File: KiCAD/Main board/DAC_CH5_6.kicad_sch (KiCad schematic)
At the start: 51 parts, among them U1 PCM1789-Q1, U3 OPA1632DR, U4 OPA1632DR

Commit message: Worked a bit on the main board
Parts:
- removed R1 (x4): 22R, Resistor_SMD:R_0805_2012Metric, symbol Device:R
- removed unit 1 of U1
- added R100: 22R, Resistor_SMD:R_Array_Convex_4x0402, symbol Device:R_Pack04
- added unit 1 of U1
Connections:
- net +3.3V: now also U1.6 (VDD)
- net AMUTEI: now also U1.17 (AMUTEI)
- net BCK: now also R100.6 (R3.2)
- net DIN: now also R100.7 (R2.2)
- net GND: now also U1.10 (AGND1), U1.15 (AGND2), U1.23 (MS/ADR0/RSV), U1.24 (ADR5/ADR1/RSV), U1.7 (DGND)
- net LRCK: now also R100.5 (R4.2)
- net MC/SCL/FMT: now also U1.20 (MODE)
- net MD/SDA/DEMP: now also U1.22 (MC/SCL/FMT)
- net MODE: now also U1.21 (MD/SDA/DEMP)
- net RST: now also U1.4 (RST)
- net SCKI: now also R100.8 (R1.2)
- net at C1.1, C3.1, R34.1: now also U1.16 (VCC2)
- net at R20.1: now also U1.13 (VOUTR+)
- net at C2.1, C5.1, R33.1: now also U1.8 (VCC1)
- net at R21.1: now also U1.14 (VOUTR-)
- net at R16.1: now also U1.11 (VOUTL-)
- net at R12.1: now also U1.12 (VOUTL+)
- new net: R100.4 (R4.1), U1.1 (LRCK)
- new net: R100.3 (R3.1), U1.2 (BCK)
- new net: R100.2 (R2.1), U1.3 (DIN)
- new net: R100.1 (R1.1), U1.5 (SCKI)
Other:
- note added: "Location? FPGA/IC?"
- note added: "NOT UP TO DATE, COPY FROM CH1_2"

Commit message: Worked on main board
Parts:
- removed C1, C20, C22, C23, C24, C28, C30, C4, C5: 22uF, Capacitor_THT:CP_Radial_D5.0mm_P2.00mm, symbol Device:C_Polarized
- removed C10, C17: 680p, Capacitor_SMD:C_0805_2012Metric, symbol Device:C
- removed C11, C18: 680, Capacitor_SMD:C_0805_2012Metric, symbol Device:C
- removed C12, C27: 2.2n, Capacitor_SMD:C_0805_2012Metric, symbol Device:C
- removed C15, C16, C21, C25, C26: 100nF, Capacitor_SMD:C_0805_2012Metric, symbol Device:C
- removed C19, C2, C3, C35: 100n, Capacitor_SMD:C_0805_2012Metric, symbol Device:C
- removed R100: 22R, Resistor_SMD:R_Array_Convex_4x0402, symbol Device:R_Pack04
- removed R12, R16, R20, R21: 1k, Resistor_SMD:R_0805_2012Metric, symbol Device:R
- removed R13, R17, R22, R23: 4.7k, Resistor_SMD:R_0805_2012Metric, symbol Device:R
- removed R14, R15, R30, R37: 39, Resistor_SMD:R_0805_2012Metric, symbol Device:R
- removed R24, R31, R32, R33, R34, R35, R36, R38: 10, Resistor_SMD:R_0805_2012Metric, symbol Device:R
- removed U1: PCM1789, Package_SO:TSSOP-24_4.4x7.8mm_P0.65mm, symbol Audio-DSP:PCM1789
- removed U3, U4: OPA1632DR, Audio_DSP:VSSOP-8_3.0x3.0mm_P0.65_TP1.8x1.5, symbol Audio-DSP:OPA1632DR
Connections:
- no-connect marks 3 -> 0
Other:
- note removed: "Location? FPGA/IC?"

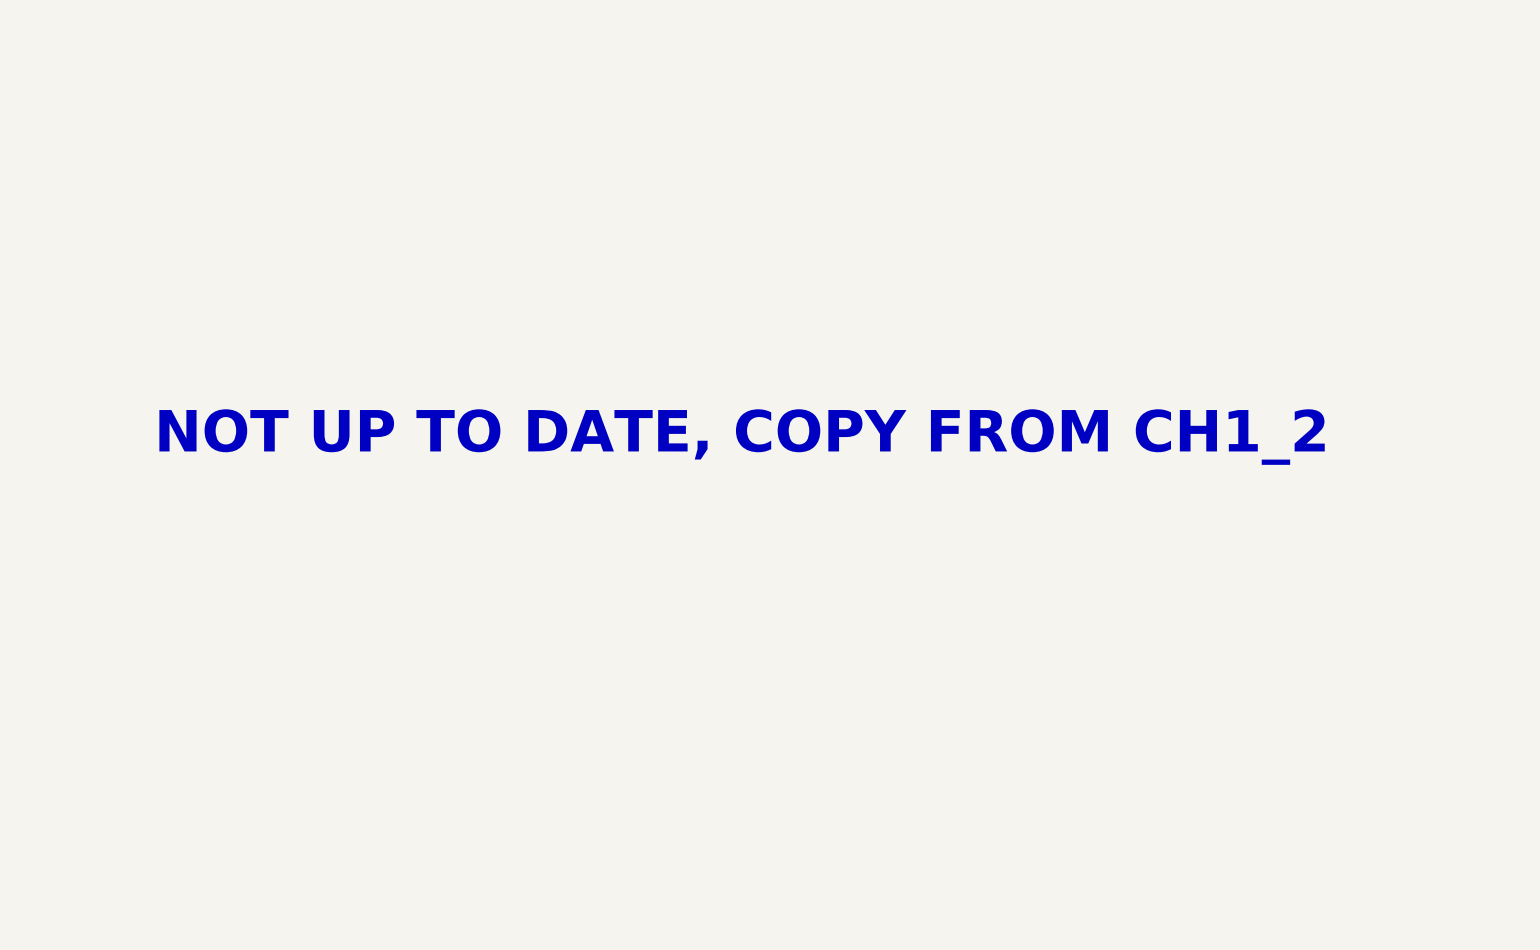
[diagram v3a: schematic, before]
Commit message: Worked on SDD, main board schematic and LTspice discrete linear regulator
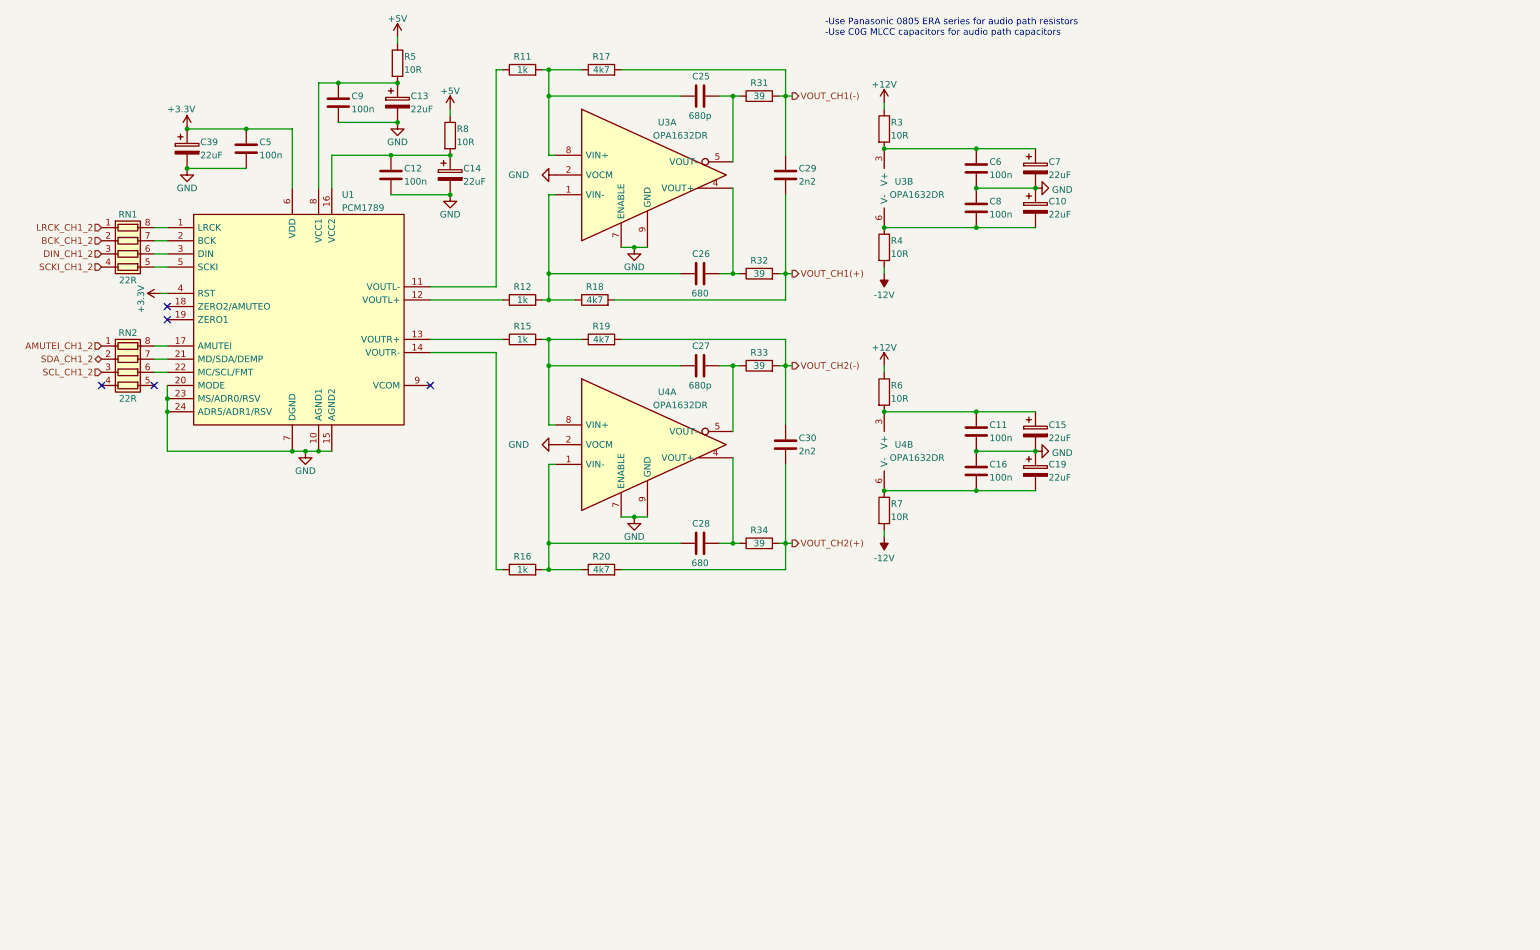
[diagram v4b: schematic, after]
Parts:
- added C10, C13, C14, C15, C19, C39, C7: 22uF, Capacitor_THT:CP_Radial_D5.0mm_P2.00mm, symbol Device:C_Polarized
- added C11, C12, C16, C5, C6, C8, C9: 100n, Capacitor_SMD:C_0402_1005Metric, symbol Device:C
- added C25, C27: 680p, Capacitor_SMD:C_0805_2012Metric, symbol Device:C
- added C26, C28: 680, Capacitor_SMD:C_0805_2012Metric, symbol Device:C
- added C29, C30: 2n2, Capacitor_SMD:C_0805_2012Metric, symbol Device:C
- added R11, R12, R15, R16: 1k, Resistor_SMD:R_0805_2012Metric, symbol Device:R
- added R17, R18, R19, R20: 4k7, Resistor_SMD:R_0805_2012Metric, symbol Device:R
- added R3, R4, R5, R6, R7, R8: 10R, Resistor_SMD:R_0805_2012Metric, symbol Device:R
- added R31, R32, R33, R34: 39, Resistor_SMD:R_0805_2012Metric, symbol Device:R
- added RN1, RN2: 22R, Resistor_SMD:R_Array_Convex_4x0402, symbol Device:R_Pack04
- added U1: PCM1789, Package_SO:TSSOP-24_4.4x7.8mm_P0.65mm, symbol Audio_DSP:PCM1789
- added U3, U4: OPA1632DR, Audio-DSP:VSSOP-8_3.0x3.0mm_P0.65_TP1.8x1.5, symbol Audio-DSP:OPA1632DR
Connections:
- new net: R15.1, U1.13 (VOUTR+)
- new net: C27.1, R15.2, R19.1, U4.8 (VIN+)
- new net: C27.2, R33.1, U4.5 (VOUT-)
- new net: R11.1, U1.11 (VOUTL-)
- new net: C25.1, R11.2, R17.1, U3.8 (VIN+)
- new net: C25.2, R31.1, U3.5 (VOUT-)
- new net: RN1.8 (R1.2), U1.1 (LRCK)
- new net: R12.1, U1.12 (VOUTL+)
- new net: R16.1, U1.14 (VOUTR-)
- new net: C12.1, C14.1, R8.2, U1.16 (VCC2)
- new net: RN2.8 (R1.2), U1.17 (AMUTEI)
- new net: RN1.7 (R2.2), U1.2 (BCK)
- new net: RN2.7 (R2.2), U1.21 (MD/SDA/DEMP)
- new net: RN2.6 (R3.2), U1.22 (MC/SCL/FMT)
- new net: RN1.6 (R3.2), U1.3 (DIN)
- new net: RN1.5 (R4.2), U1.5 (SCKI)
- new net: C13.1, C9.1, R5.2, U1.8 (VCC1)
- new net: C26.1, R12.2, R18.1, U3.1 (VIN-)
- new net: C26.2, R32.1, U3.4 (VOUT+)
- new net: C6.1, C7.1, R3.2, U3.3 (V+)
- new net: C28.1, R16.2, R20.1, U4.1 (VIN-)
- new net: C28.2, R34.1, U4.4 (VOUT+)
- new net: C11.1, C15.1, R6.2, U4.3 (V+)
- new net: C16.2, C19.2, R7.1, U4.6 (V-)
- new net: C10.2, C8.2, R4.1, U3.6 (V-)
- new net +12V: R3.1, R6.1
- new net +3.3V: C39.1, C5.1, U1.4 (RST), U1.6 (VDD)
- new net +5V: R5.1, R8.1
- new net -12V: R4.2, R7.2
- new net AMUTEI_CH1_2: RN2.1 (R1.1)
- new net BCK_CH1_2: RN1.2 (R2.1)
- new net DIN_CH1_2: RN1.3 (R3.1)
- new net GND: C10.1, C11.2, C12.2, C13.2, C14.2, C15.2, C16.1, C19.1, C39.2, C5.2, C6.2, C7.2, C8.1, C9.2, U1.10 (AGND1), U1.15 (AGND2), U1.20 (MODE), U1.23 (MS/ADR0/RSV), U1.24 (ADR5/ADR1/RSV), U1.7 (DGND), U3.2 (VOCM), U3.7 (ENABLE), U3.9 (GND), U4.2 (VOCM), U4.7 (ENABLE), U4.9 (GND)
- new net LRCK_CH1_2: RN1.1 (R1.1)
- new net SCKI_CH1_2: RN1.4 (R4.1)
- new net SCL_CH1_2: RN2.3 (R3.1)
- new net SDA_CH1_2: RN2.2 (R2.1)
- new net VOUT_CH1(+): C29.2, R18.2, R32.2
- new net VOUT_CH1(-): C29.1, R17.2, R31.2
- new net VOUT_CH2(+): C30.2, R20.2, R34.2
- new net VOUT_CH2(-): C30.1, R19.2, R33.2
- no-connect marks 0 -> 5
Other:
- note added: "-Use Panasonic 0805 ERA series for audio path resistors -Use C0G MLCC capacitors for audio path capacitors"
- note removed: "NOT UP TO DATE, COPY FROM CH1_2"

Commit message: Worked on main board schematic and PCB, added symbols to symbol library
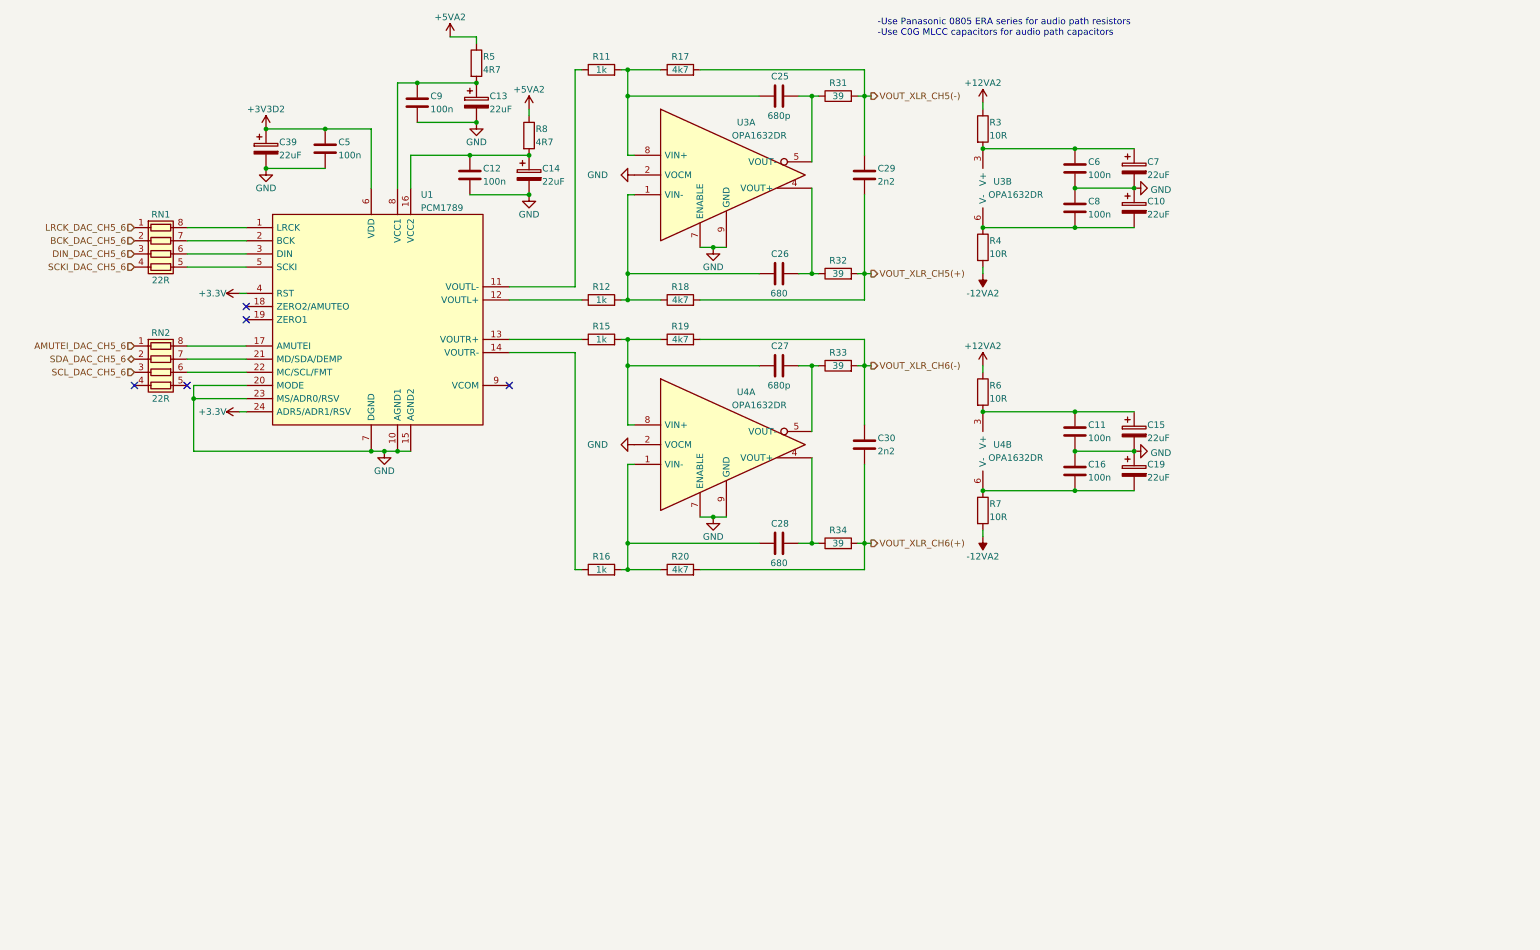
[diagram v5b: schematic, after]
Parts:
- R5, R8: value 10R -> 4R7
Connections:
- net +3.3V: now also U1.24 (ADR5/ADR1/RSV); no longer C39.1, C5.1, U1.6 (VDD)
- net GND: no longer U1.24 (ADR5/ADR1/RSV)
- net +12V renamed +12VA2
- net +5V renamed +5VA2
- net -12V renamed -12VA2
- net AMUTEI_CH1_2 renamed AMUTEI_DAC_CH5_6
- net BCK_CH1_2 renamed BCK_DAC_CH5_6
- net DIN_CH1_2 renamed DIN_DAC_CH5_6
- net LRCK_CH1_2 renamed LRCK_DAC_CH5_6
- net SCKI_CH1_2 renamed SCKI_DAC_CH5_6
- net SCL_CH1_2 renamed SCL_DAC_CH5_6
- net SDA_CH1_2 renamed SDA_DAC_CH5_6
- net VOUT_CH1(+) renamed VOUT_XLR_CH5(+)
- net VOUT_CH1(-) renamed VOUT_XLR_CH5(-)
- net VOUT_CH2(+) renamed VOUT_XLR_CH6(+)
- net VOUT_CH2(-) renamed VOUT_XLR_CH6(-)
- new net +3V3D2: C39.1, C5.1, U1.6 (VDD)
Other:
- moved on the sheet: C10, C11, C12, C13, C14, C15, C16, C19, C25, C26, C27, C28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

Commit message: Worked in main board
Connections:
- net +3.3V is gone; now on net +3V3D2: U1.24 (ADR5/ADR1/RSV), U1.4 (RST)
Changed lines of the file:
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@@
-    (stroke (width 0) (type default))
-  )
-  (wire (pts (xy 53.34 67.31) (xy 54.61 67.31))
     (stroke (width 0) (type default))
   )
@@
   )
   (wire (pts (xy 196.85 30.48) (xy 196.85 31.75))
-    (stroke (width 0) (type default))
-  )
-  (wire (pts (xy 53.34 90.17) (xy 54.61 90.17))
     (stroke (width 0) (type default))
   )
@@
     )
   )
-  (symbol (lib_id "power:+3.3V") (at 53.34 67.31 90) (unit 1)
-    (in_bom yes) (on_board yes) (dnp no)
-    (property "Reference" "#PWR0137" (at 57.15 67.31 0)
-      (effects (font (size 1.27 1.27)) hide)
-    )
-    (property "Value" "+3.3V" (at 50.8 67.31 90)
-      (effects (font (size 1.27 1.27)) (justify left))
-    )
-    (property "Footprint" "" (at 53.34 67.31 0)
-      (effects (font (size 1.27 1.27)) hide)
-    )
-    (property "Datasheet" "" (at 53.34 67.31 0)
-      (effects (font (size 1.27 1.27)) hide)
-    )
-    (pin "1")
-    (instances
-      (project "Main board"
-        (path "/2f8cbac6-fd11-4240-8e40-3bb6952a0324/03c234da-ad6d-41dc-b0ec-5880e5376fd2"
-          (reference "#PWR0137") (unit 1)
-        )
-        (path "/2f8cbac6-fd11-4240-8e40-3bb6952a0324/05d59304-dfac-45e1-85e6-83cda4d81484"
-          (reference "#PWR011") (unit 1)
+  (symbol (lib_id "Audio_DSP:+3V3D2") (at 54.61 67.31 90) (unit 1)
+    (in_bom no) (on_board no) (dnp no)
+    (property "Reference" "#PWR0106" (at 57.15 67.31 0)
+      (effects (font (size 1.27 1.27)) hide)
+    )
+    (property "Value" "+3V3D2" (at 52.07 67.31 90)
+      (effects (font (size 1.27 1.27)) (justify left))
+    )
+    (property "Footprint" "" (at 54.61 67.31 0)
+      (effects (font (size 1.27 1.27)) hide)
+    )
+    (property "Datasheet" "" (at 54.61 67.31 0)
+      (effects (font (size 1.27 1.27)) hide)
+    )
+    (pin "1")
+    (instances
+      (project "Main board"
+        (path "/2f8cbac6-fd11-4240-8e40-3bb6952a0324/fc272ee1-9060-465b-85c1-b8364d68deb3"
+          (reference "#PWR0106") (unit 1)
+        )
+        (path "/2f8cbac6-fd11-4240-8e40-3bb6952a0324/05d59304-dfac-45e1-85e6-83cda4d81484"
+          (reference "#PWR0174") (unit 1)
         )
         (path "/2f8cbac6-fd11-4240-8e40-3bb6952a0324/5bd992f9-4f10-40f4-8ffe-2d7c60250f66"
@@
         (path "/2f8cbac6-fd11-4240-8e40-3bb6952a0324/5bd992f9-4f10-40f4-8ffe-2d7c60250f66"
           (reference "#PWR041") (unit 1)
+        )
+      )
+    )
+  )
+  (symbol (lib_id "Audio_DSP:+3V3D2") (at 54.61 90.17 90) (unit 1)
+    (in_bom no) (on_board no) (dnp no)
+    (property "Reference" "#PWR0106" (at 57.15 90.17 0)
+      (effects (font (size 1.27 1.27)) hide)
+    )
+    (property "Value" "+3V3D2" (at 52.07 90.17 90)
+      (effects (font (size 1.27 1.27)) (justify left))
+    )
+    (property "Footprint" "" (at 54.61 90.17 0)
+      (effects (font (size 1.27 1.27)) hide)
+    )
+    (property "Datasheet" "" (at 54.61 90.17 0)
+      (effects (font (size 1.27 1.27)) hide)
+    )
+    (pin "1")
+    (instances
+      (project "Main board"
+        (path "/2f8cbac6-fd11-4240-8e40-3bb6952a0324/fc272ee1-9060-465b-85c1-b8364d68deb3"
+          (reference "#PWR0106") (unit 1)
+        )
+        (path "/2f8cbac6-fd11-4240-8e40-3bb6952a0324/05d59304-dfac-45e1-85e6-83cda4d81484"
+          (reference "#PWR0174") (unit 1)
+        )
+        (path "/2f8cbac6-fd11-4240-8e40-3bb6952a0324/5bd992f9-4f10-40f4-8ffe-2d7c60250f66"
+          (reference "#PWR045") (unit 1)
         )
       )
@@
         )
       )
-    )
-  )
-  (symbol (lib_id "power:+3.3V") (at 53.34 90.17 90) (unit 1)
-    (in_bom yes) (on_board yes) (dnp no)
-    (property "Reference" "#PWR0137" (at 57.15 90.17 0)
-      (effects (font (size 1.27 1.27)) hide)
-    )
-    (property "Value" "+3.3V" (at 50.8 90.17 90)
-      (effects (font (size 1.27 1.27)) (justify left))
-    )
-    (property "Footprint" "" (at 53.34 90.17 0)
-      (effects (font (size 1.27 1.27)) hide)
-    )
-    (property "Datasheet" "" (at 53.34 90.17 0)
-      (effects (font (size 1.27 1.27)) hide)
-    )
-    (pin "1")
-    (instances
-      (project "Main board"
-        (path "/2f8cbac6-fd11-4240-8e40-3bb6952a0324/03c234da-ad6d-41dc-b0ec-5880e5376fd2"
-          (reference "#PWR0137") (unit 1)
-        )
-        (path "/2f8cbac6-fd11-4240-8e40-3bb6952a0324/05d59304-dfac-45e1-85e6-83cda4d81484"
-          (reference "#PWR011") (unit 1)
-        )
-        (path "/2f8cbac6-fd11-4240-8e40-3bb6952a0324/5bd992f9-4f10-40f4-8ffe-2d7c60250f66"
-          (reference "#PWR045") (unit 1)
-        )
-      )

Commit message: Worked on main board schematic
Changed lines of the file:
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@@
-    (stroke (width 0) (type default))
-  )
-  (wire (pts (xy 99.06 17.78) (xy 93.98 17.78))
     (stroke (width 0) (type default))
   )
@@
     (stroke (width 0) (type default))
   )
-  (wire (pts (xy 109.22 33.02) (xy 109.22 31.75))
-    (stroke (width 0) (type default))
-  )
   (wire (pts (xy 134.62 68.58) (xy 128.27 68.58))
     (stroke (width 0) (type default))
@@
   )
   (wire (pts (xy 128.27 29.21) (xy 128.27 40.64))
-    (stroke (width 0) (type default))
-  )
-  (wire (pts (xy 99.06 19.05) (xy 99.06 17.78))
     (stroke (width 0) (type default))
   )
@@
       (effects (font (size 1.27 1.27)) hide)
     )
-    (property "Value" "GND" (at 124.46 96.52 90)
+    (property "Value" "GND" (at 127 96.52 90)
       (effects (font (size 1.27 1.27)) (justify right))
     )
@@
     )
   )
-  (symbol (lib_id "Audio-DSP:+5VA2") (at 93.98 17.78 0) (unit 1)
+  (symbol (lib_id "Audio-DSP:+5VA2") (at 99.06 19.05 0) (unit 1)
     (in_bom no) (on_board no) (dnp no) (fields_autoplaced)
-    (property "Reference" "#PWR049" (at 93.98 20.32 0)
-      (effects (font (size 1.27 1.27)) hide)
-    )
-    (property "Value" "+5VA2" (at 93.98 13.97 0)
-      (effects (font (size 1.27 1.27)))
-    )
-    (property "Footprint" "" (at 93.98 17.78 0)
-      (effects (font (size 1.27 1.27)) hide)
-    )
-    (property "Datasheet" "" (at 93.98 17.78 0)
+    (property "Reference" "#PWR049" (at 99.06 21.59 0)
+      (effects (font (size 1.27 1.27)) hide)
+    )
+    (property "Value" "+5VA2" (at 99.06 15.24 0)
+      (effects (font (size 1.27 1.27)))
+    )
+    (property "Footprint" "" (at 99.06 19.05 0)
+      (effects (font (size 1.27 1.27)) hide)
+    )
+    (property "Datasheet" "" (at 99.06 19.05 0)
       (effects (font (size 1.27 1.27)) hide)
     )
@@
       (effects (font (size 1.27 1.27)) hide)
     )
-    (property "Value" "GND" (at 124.46 44.45 90)
+    (property "Value" "GND" (at 127 44.45 90)
       (effects (font (size 1.27 1.27)) (justify right))
     )
@@
     )
   )
-  (symbol (lib_id "Audio-DSP:+5VA2") (at 109.22 31.75 0) (unit 1)
+  (symbol (lib_id "Audio-DSP:+5VA2") (at 109.22 33.02 0) (unit 1)
     (in_bom no) (on_board no) (dnp no) (fields_autoplaced)
-    (property "Reference" "#PWR049" (at 109.22 34.29 0)
-      (effects (font (size 1.27 1.27)) hide)
-    )
-    (property "Value" "+5VA2" (at 109.22 27.94 0)
-      (effects (font (size 1.27 1.27)))
-    )
-    (property "Footprint" "" (at 109.22 31.75 0)
-      (effects (font (size 1.27 1.27)) hide)
-    )
-    (property "Datasheet" "" (at 109.22 31.75 0)
-      (effects (font (size 1.27 1.27)) hide)
-    )
+    (property "Reference" "#PWR049" (at 109.22 35.56 0)
+      (effects (font (size 1.27 1.27)) hide)
+    )
+    (property "Value" "+5VA2" (at 109.22 29.21 0)
+      (effects (font (size 1.27 1.27)))
+    )
+    (property "Footprint" "" (at 109.22 33.02 0)
+      (effects (font (size 1.27 1.27)) hide)
+    )
+    (property "Datasheet" "" (at 109.22 33.02 0)
+      (effects (font (size 1.27 1.27)) hide)
+    )
